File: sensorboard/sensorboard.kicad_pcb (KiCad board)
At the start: 4 copper layers, 100 x 50 mm, 236 parts, among them J1 Conn_01x03, J10 Conn_01x02_Male, J11 Conn_01x05_Male, J12 Conn_01x03, J13 Conn_01x03, J14 USB_C_Receptacle_USB2.0, J2 Conn_01x03, J3 Conn_01x03, J4 Conn_01x03, J5 Conn_01x03, J6 Conn_01x03, J7 Conn_01x03, J8 Conn_01x03, J9 Conn_01x02_Male, Q1 MMDT2222A, U1 ESP32-PICO-D4, U10 MAX31856, U11 MAX31856, U12 RT9025-25GSP, U13 ADS1219, U14 ADS1219, U15 ADS1219, U16 MAX31856, U17 MAX31856, U18 MAX31856, U19 LTC4411, U2 LTC4411, U20 SN65HVD230, U3 TPS61092RSAR, U4 MAX31856, U5 MAX31856, U6 MAX31856, U7 MAX31856, U8 CP2102-GMR-QFN28, U9 MAX31856

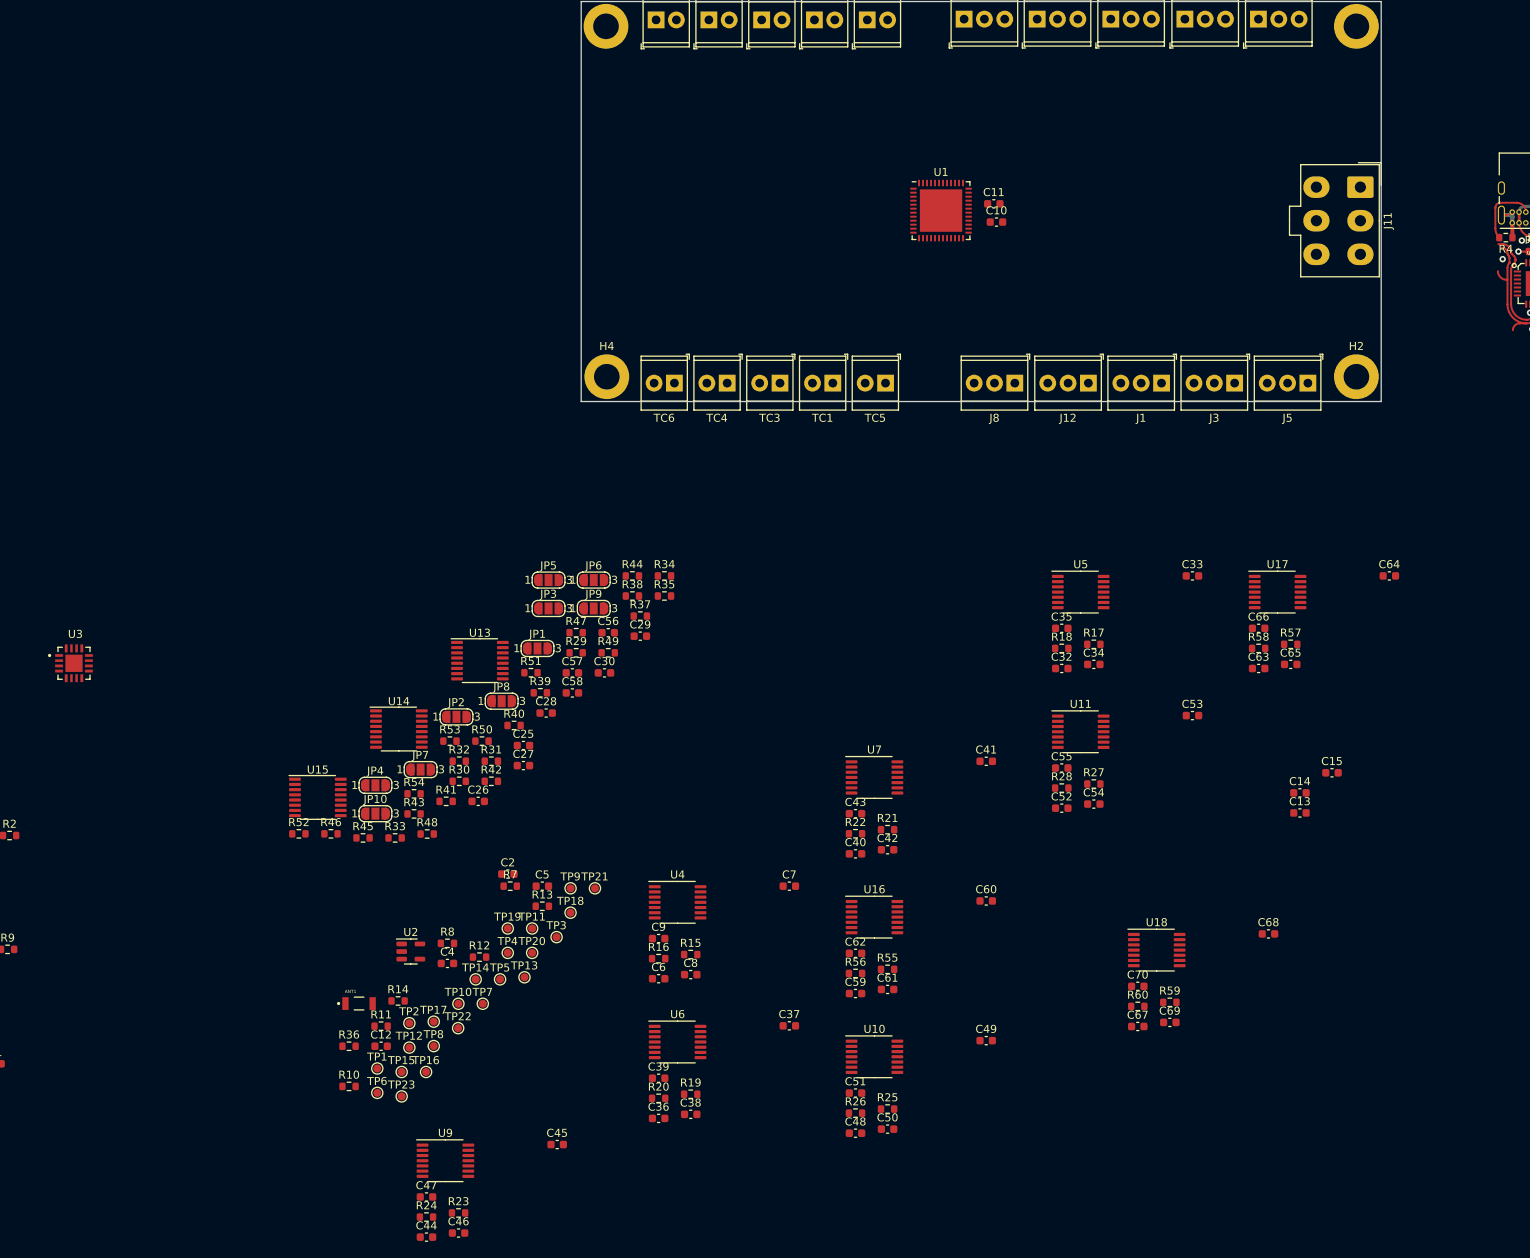
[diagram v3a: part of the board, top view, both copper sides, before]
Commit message: antenna and thermocouple prelim
Preliminary layout for thermocouples and antenna structure done
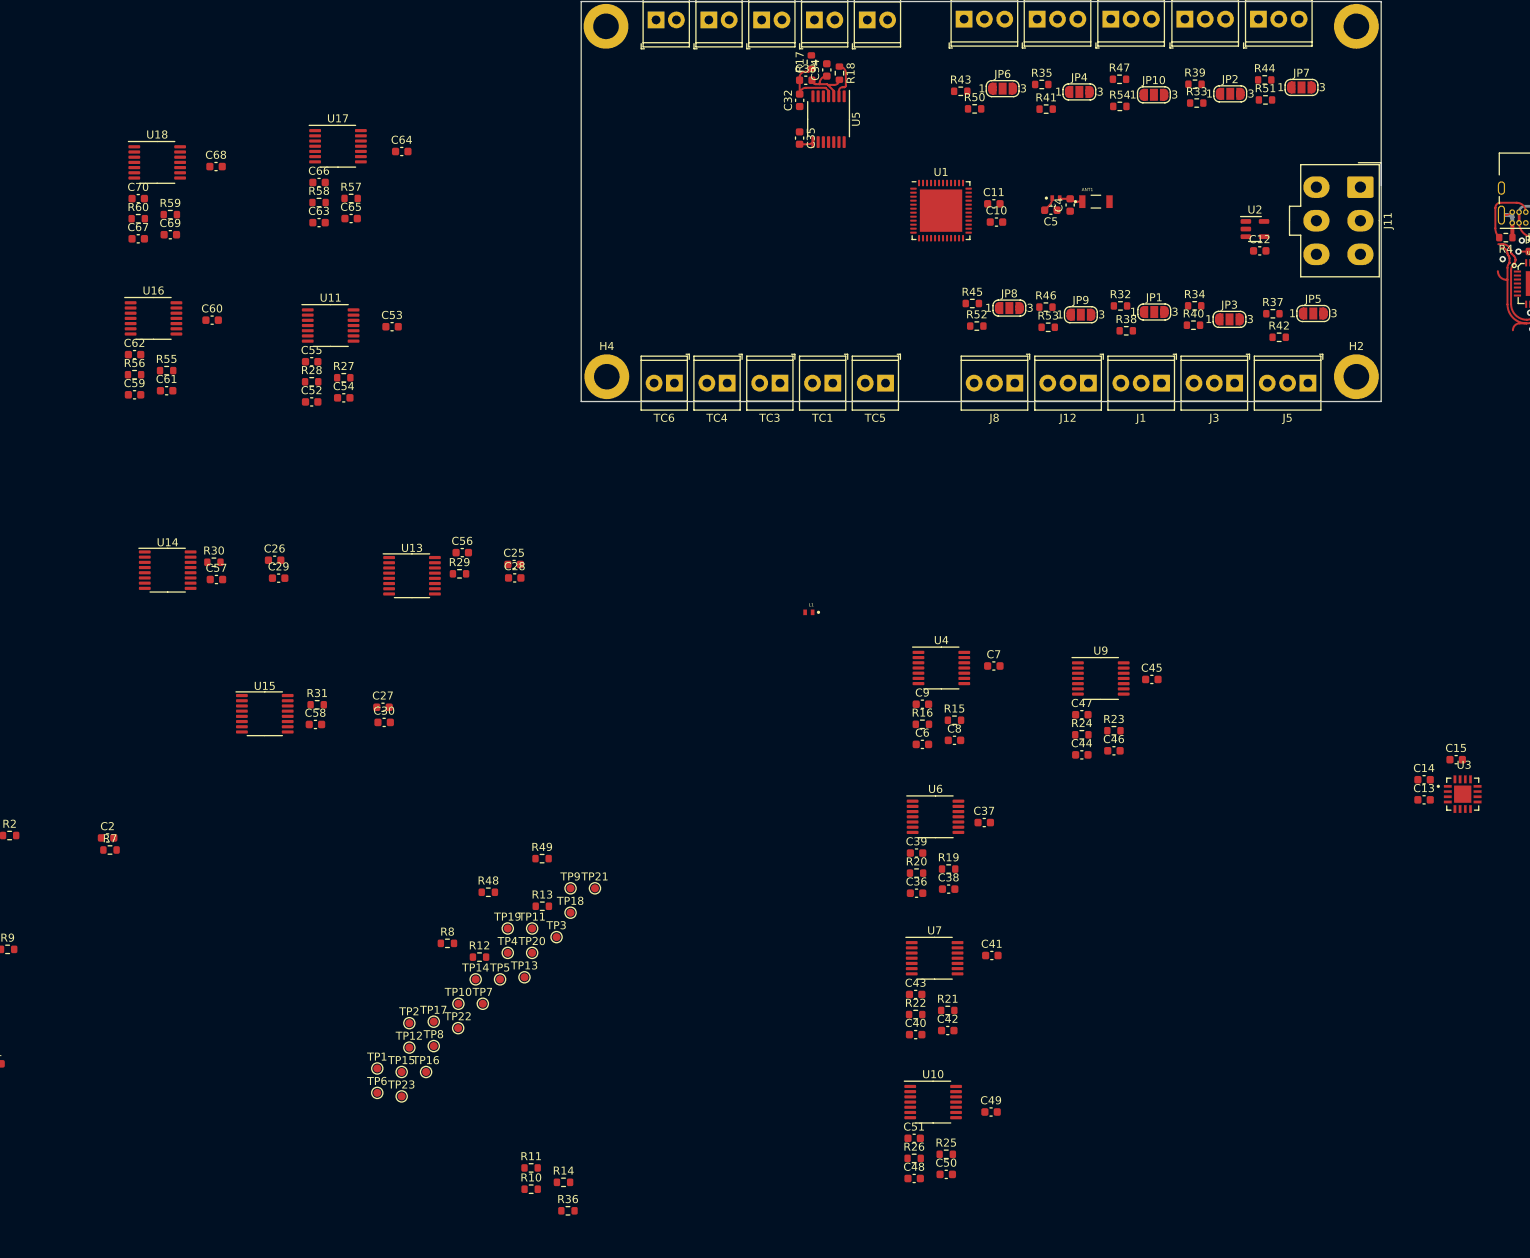
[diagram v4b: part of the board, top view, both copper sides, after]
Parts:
- added L1: 6.8uH, iclr:INDC1006X60N, F.Cu at (128.5, 106.3)
- added L2: LQG15WZ1N8B02D, iclr:INDC1006X60N, F.Cu at (159.3, 54.6)
- moved U3 174.4 mm to (210.2, 129.1)
- moved C68 162.8 mm to (54.4, 50.6)
- moved C67 159.1 mm to (44.6, 59.7)
- moved C69 159.1 mm to (48.6, 59.1)
- moved C70 159.1 mm to (44.6, 54.6)
- moved R60 159.1 mm to (44.6, 57.1)
- moved U18 159.1 mm to (47.0, 50.1)
- moved R59 159.1 mm to (48.6, 56.6)
- moved C12 148.1 mm to (184.8, 61.2)
- moved JP7 139.3 mm to (190.0, 40.7)
- moved U2 138.9 mm to (184.2, 58.4)
- moved ANT1 136.1 mm to (164.3, 55.0)
- moved R33 135.9 mm to (176.9, 42.7)
- moved C64 134.4 mm to (77.6, 48.8)
- moved JP10 132.5 mm to (171.6, 41.7)
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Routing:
- net Net-(C32-Pad2): track 0.00 -> 9.03 mm
- net Net-(C33-Pad2): track 0.00 -> 7.29 mm
- net Net-(R18-Pad1): track 0.00 -> 4.70 mm
- net unconnected-(U8-Pad22): track 4.60 -> 0.00 mm
- net Net-(R6-Pad2): track 0.00 -> 4.60 mm
- net Net-(ANT1-Pad1): track 0.00 -> 2.93 mm
- net /LNA_IN: track 0.00 -> 1.84 mm
- net Net-(R62-Pad2): track 0.00 -> 1.78 mm
- net Net-(R17-Pad2): track 1.78 -> 0.00 mm
- net +3V3: track 20.0 -> 21.8 mm

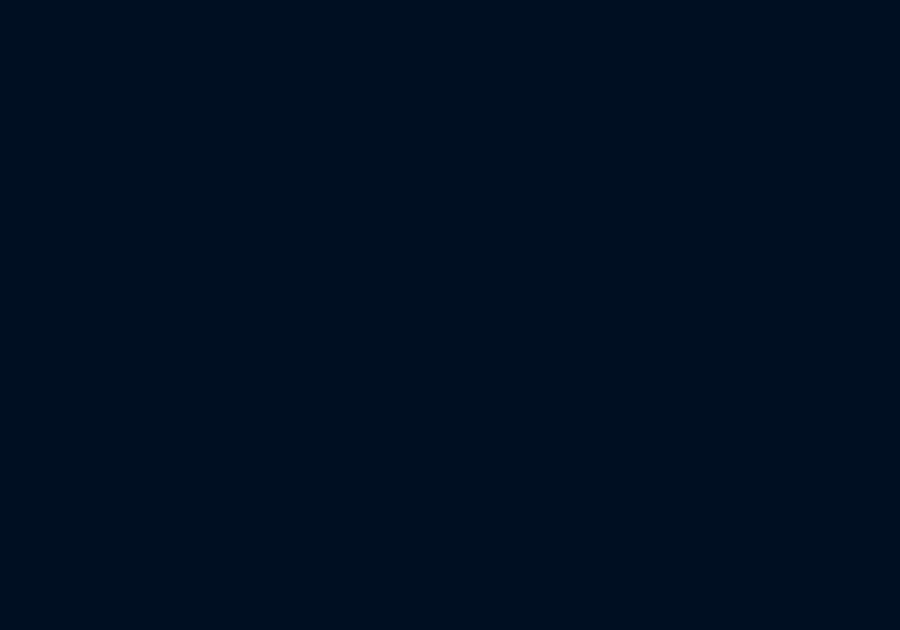
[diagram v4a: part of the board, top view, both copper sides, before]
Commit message: Changed diode fps from castellated
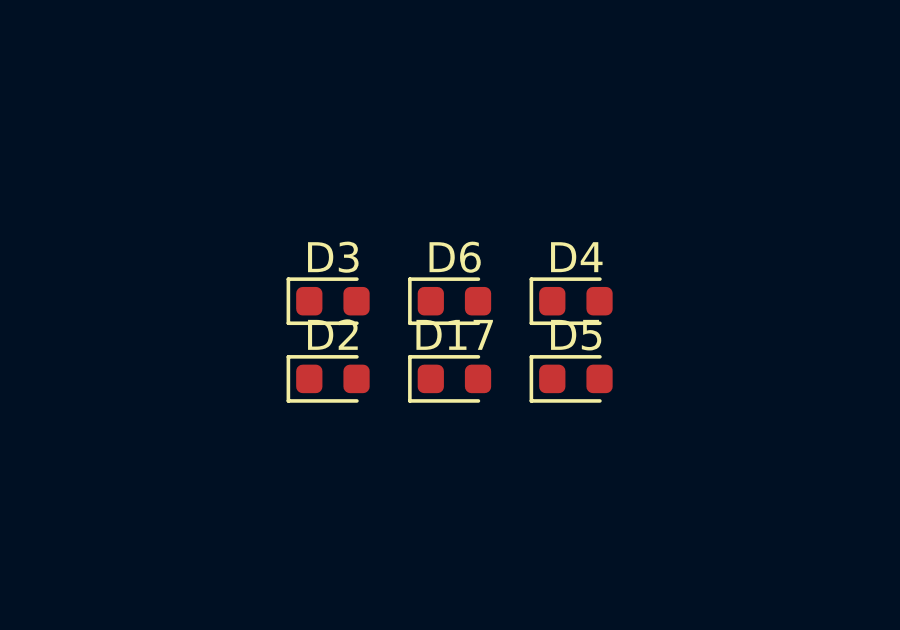
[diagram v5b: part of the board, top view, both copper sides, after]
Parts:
- added D17: USB_LED, LED_SMD:LED_0603_1608Metric, F.Cu at (114.8, 164.9)
- added D2: RX_LED, LED_SMD:LED_0603_1608Metric, F.Cu at (110.7, 164.9)
- added D3: TX_LED, LED_SMD:LED_0603_1608Metric, F.Cu at (110.7, 162.3)
- added D4: LED, LED_SMD:LED_0603_1608Metric, F.Cu at (118.8, 162.3)
- added D5: LED, LED_SMD:LED_0603_1608Metric, F.Cu at (118.8, 164.9)
- added D6: PWR_LED, LED_SMD:LED_0603_1608Metric, F.Cu at (114.8, 162.3)

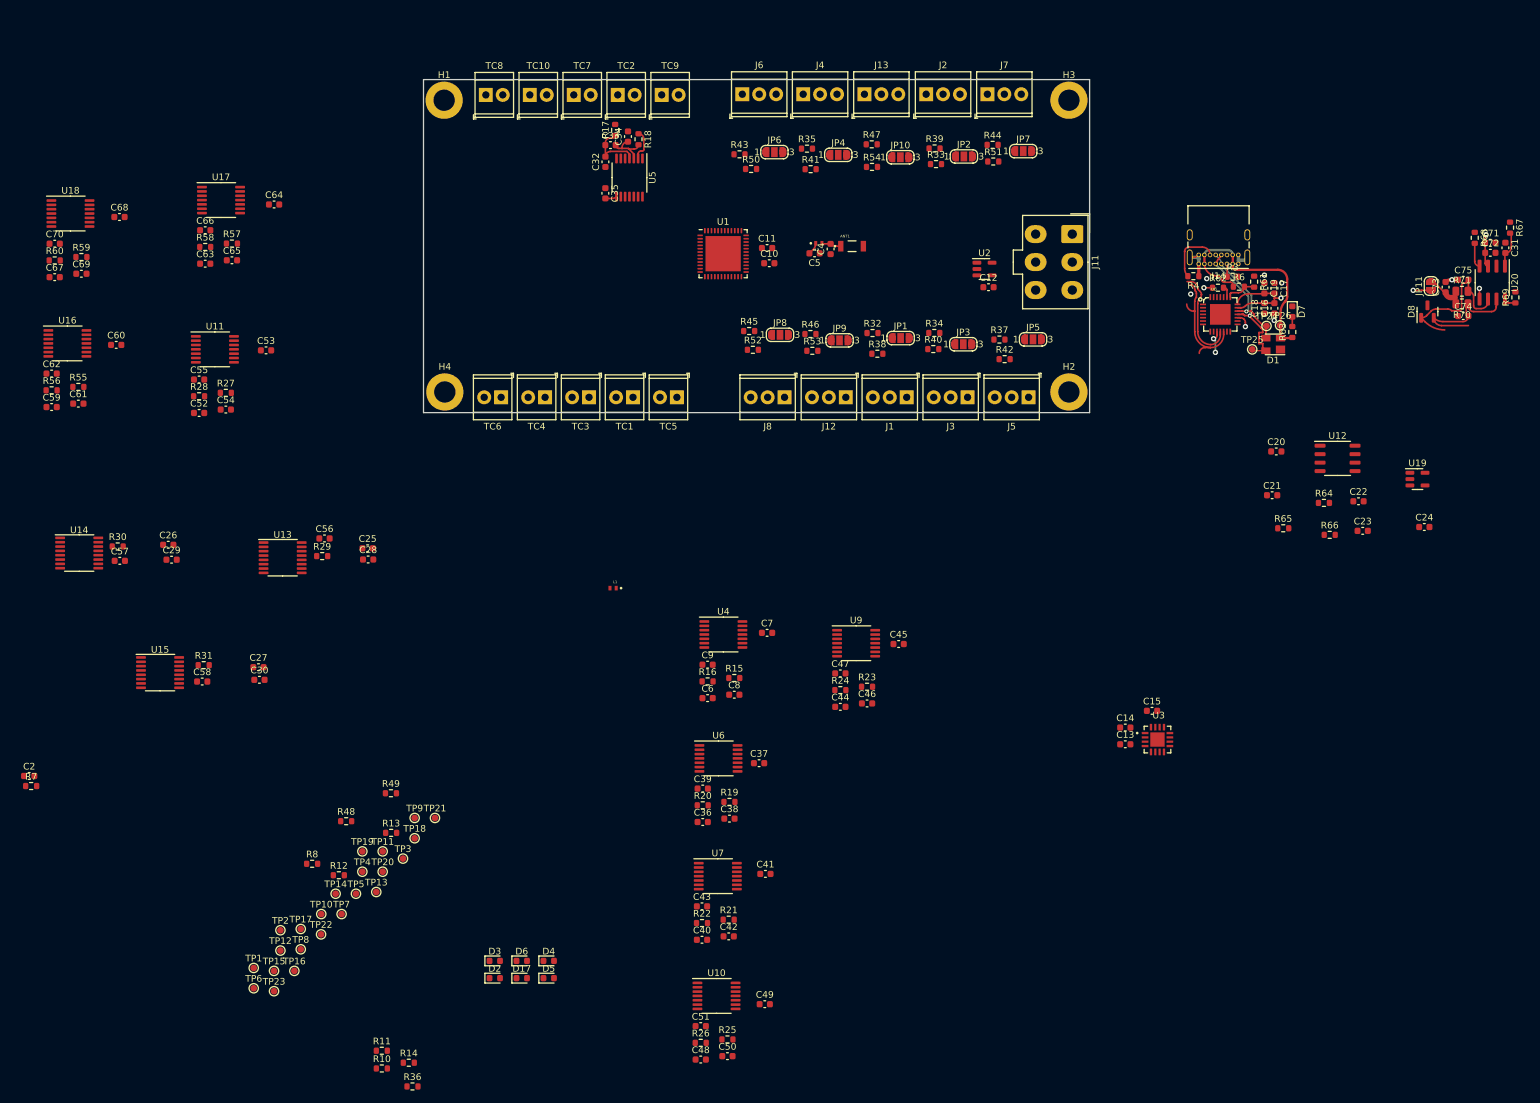
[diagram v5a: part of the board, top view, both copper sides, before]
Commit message: Thermocouple structures
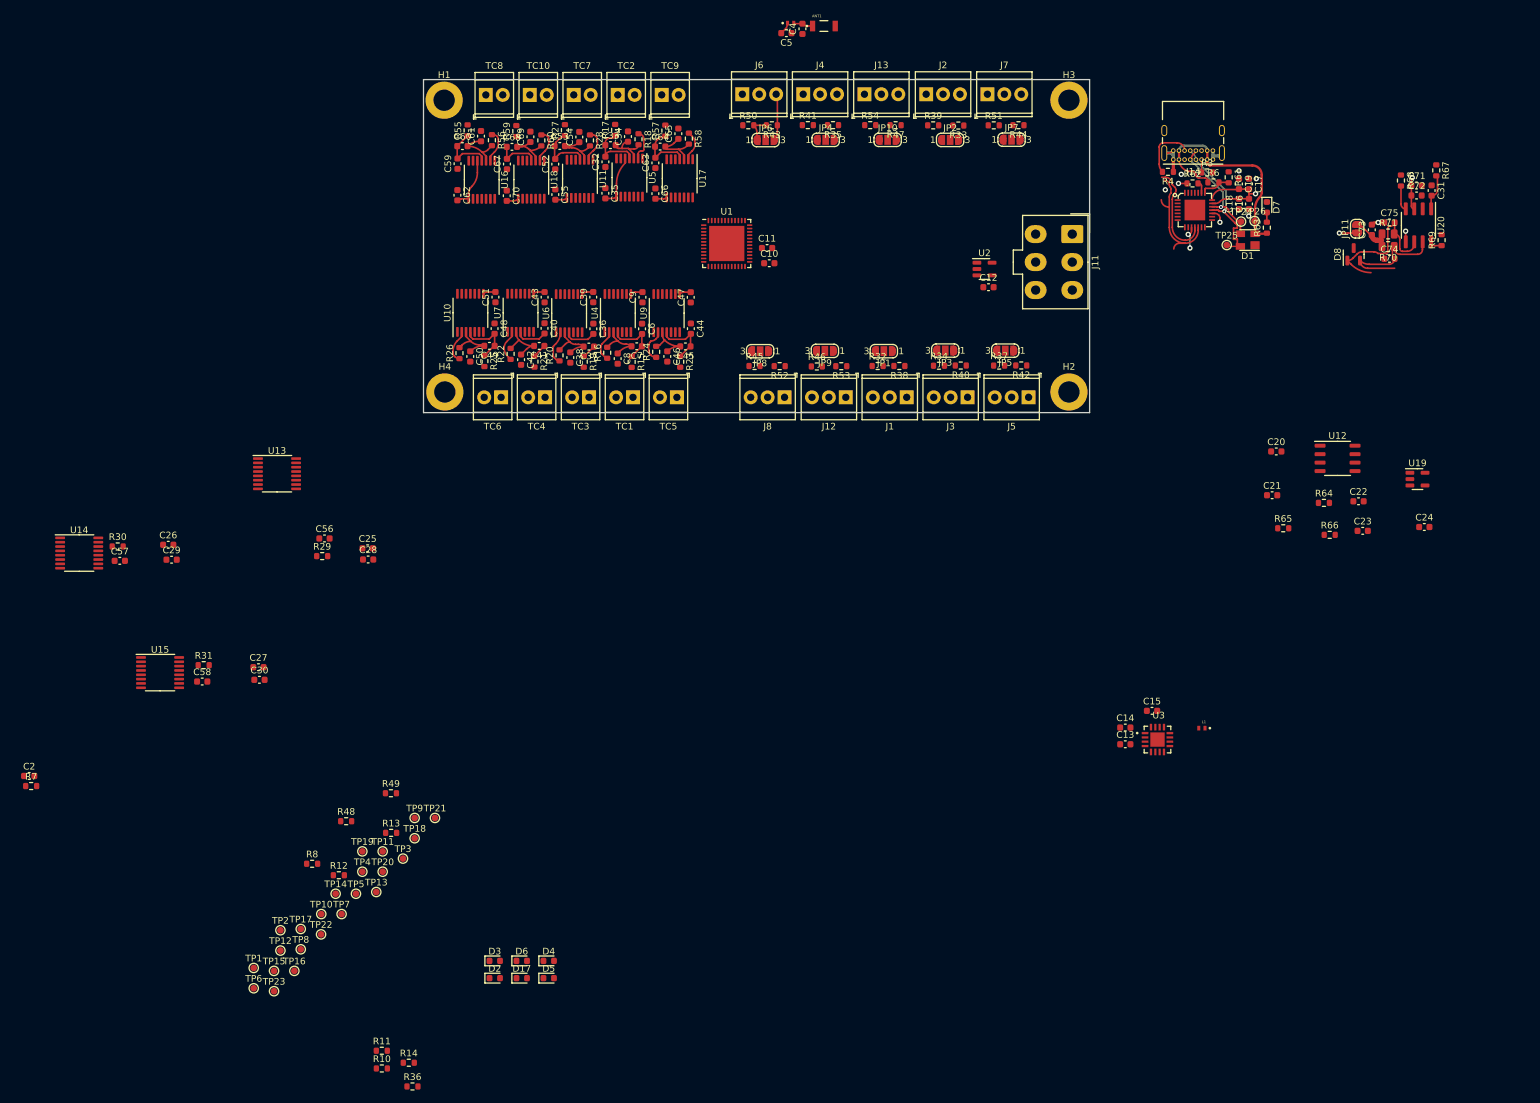
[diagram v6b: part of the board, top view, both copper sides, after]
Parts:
- moved C48 114.0 mm to (110.7, 67.4), turned to -90 degrees
- moved C51 113.7 mm to (110.8, 62.7), turned to 90 degrees
- moved C50 111.9 mm to (107.0, 71.6), turned to -90 degrees
- moved R26 109.7 mm to (105.4, 71.1), turned to 90 degrees
- moved U10 109.0 mm to (107.0, 65.0), turned to 90 degrees
- moved R25 108.2 mm to (109.1, 72.3), turned to -90 degrees
- moved C49 107.1 mm to (109.9, 70.0), turned to 180 degrees
- moved C40 94.8 mm to (118.2, 67.3), turned to -90 degrees
- moved C43 94.5 mm to (118.2, 62.7), turned to 90 degrees
- moved C42 92.0 mm to (114.7, 72.0), turned to -90 degrees
- moved L1 90.9 mm to (216.9, 127.4)
- moved R22 90.2 mm to (113.1, 71.2), turned to 90 degrees
- moved U7 89.6 mm to (114.6, 65.0), turned to 90 degrees
- moved R21 88.7 mm to (116.7, 72.3), turned to -90 degrees
- moved C41 86.2 mm to (117.4, 70.0), turned to 180 degrees
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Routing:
- net +3V3: track 21.8 -> 49.9 mm
- net Net-(C52-Pad2): track 0.00 -> 9.25 mm
- net Net-(C63-Pad2): track 0.00 -> 8.98 mm
- net Net-(C44-Pad2): track 0.00 -> 8.88 mm
- net Net-(C6-Pad2): track 0.00 -> 8.81 mm
- net Net-(C48-Pad2): track 0.00 -> 8.75 mm
- net Net-(C59-Pad2): track 0.00 -> 8.62 mm
- net Net-(C37-Pad2): track 0.00 -> 8.26 mm
- net Net-(C49-Pad2): track 0.00 -> 8.22 mm
- net Net-(C64-Pad2): track 0.00 -> 8.22 mm
- net Net-(C7-Pad2): track 0.00 -> 8.18 mm
- net Net-(C68-Pad2): track 0.00 -> 8.04 mm
- net Net-(C53-Pad2): track 0.00 -> 8.04 mm
- net Net-(C41-Pad2): track 0.00 -> 8.00 mm
- net Net-(C60-Pad2): track 0.00 -> 7.95 mm
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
